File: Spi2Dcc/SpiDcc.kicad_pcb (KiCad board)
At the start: 2 copper layers, 100 x 65 mm, 90 parts, among them P701 LED, P702 Invld cmd out, P703 Mstr SW, P704 Mstr SW bypass, P705 Bstr En Out, P706 Mstr SW out, P801 SPI, P901 Bstr 1, P902 Bstr 2, P903 Bstr 3, P904 Bstr 4, Q701 BC327-40, Q702 BC327-40, Q703 BC327-40, Q901 BC327-40, U201 LM555N, U202 74HC74, U301 74HC4053, U302 74HC32, U401 74HC163, U402 74HC04, U403 74HC163, U404 74HC193, U501 74HC590, U502 74HC75, U503 74HC153, U601 74HC595, U602 74HC165, U603 74HC595, U604 74HC165, U605 74HC595, U606 74HC165, U607 74HC595, U608 74HC165, U609 74HC595, U610 74HC165, U611 74HC595, U612 74HC165

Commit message: Changing the solder mask settings again - based on recommendation found here: http://www.360customs.de/en/2017/01/kicad-elecrow-pcb-service/
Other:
- rule pad_to_mask_clearance: 0.2 -> 0.05
- rule solder_mask_min_width: 0.2 -> 0.1
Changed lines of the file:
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@@
     (pad_size 5 5)
     (pad_drill 3.2)
-    (pad_to_mask_clearance 0.2)
-    (solder_mask_min_width 0.2)
+    (pad_to_mask_clearance 0.05)
+    (solder_mask_min_width 0.1)
     (aux_axis_origin 0 0)
     (visible_elements 7FFFFFFF)
@@
       (drillshape 0)
       (scaleselection 1)
-      (outputdirectory C:/Users/Lars.BEVELDYR/Desktop/SporskiftetBlogBilleder/))
+      (outputdirectory Gerber/))
   )
   (net 0 "")

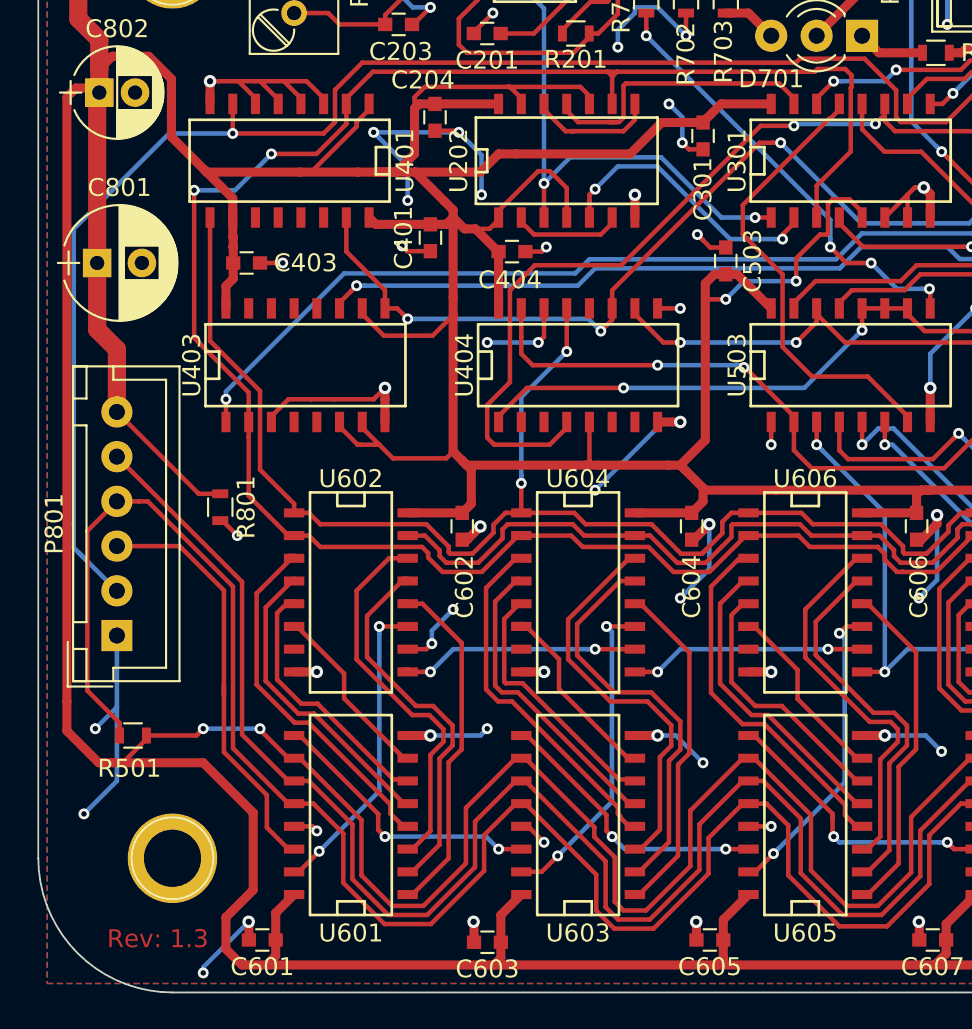
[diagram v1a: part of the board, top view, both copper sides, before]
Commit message: fix command length bits swapped. Connect mounting hole pads to GND.
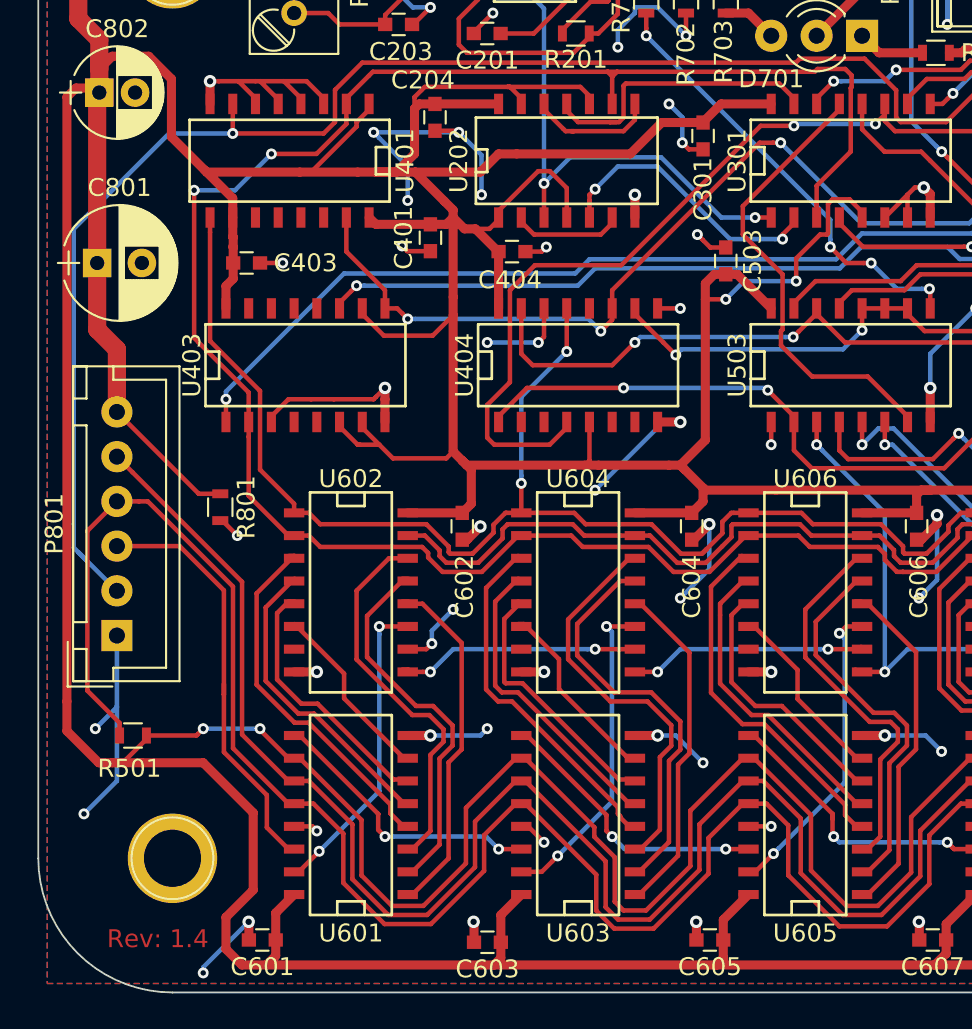
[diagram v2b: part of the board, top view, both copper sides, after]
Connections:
- REF** pad 1: (no net) -> GND (x4)
- U404 pad 1: /DCC State Machine/CMD_LENGTH_BIT_1 -> /Command Register/CMD_LENGTH_BIT_1
- U404 pad 10: /Command Register/CMD_LENGTH_BIT_0 -> /Command Register/CMD_LENGTH_BIT_2
- U404 pad 15: /DCC State Machine/CMD_LENGTH_BIT_0 -> /Command Register/CMD_LENGTH_BIT_0
- U502 pad 10: /DCC State Machine/CMD_LENGTH_BIT_1 -> /Command Register/CMD_LENGTH_BIT_2
- U502 pad 15: /DCC State Machine/CMD_LENGTH_BIT_0 -> /Command Register/CMD_LENGTH_BIT_1
- U503 pad 10: /DCC State Machine/CMD_LENGTH_BIT_1 -> /Command Register/CMD_LENGTH_BIT_2
- U503 pad 11: /DCC State Machine/CMD_LENGTH_BIT_1 -> /Command Register/CMD_LENGTH_BIT_2
- U503 pad 12: /DCC State Machine/CMD_LENGTH_BIT_1 -> /Command Register/CMD_LENGTH_BIT_2
- U503 pad 2: /DCC State Machine/CMD_LENGTH_BIT_0 -> /Command Register/CMD_LENGTH_BIT_1
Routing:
- net /DCC State Machine/CMD_LENGTH_BIT_1: track 47.8 -> 0.00 mm, vias 2 -> 0
- net /DCC State Machine/CMD_LENGTH_BIT_0: track 42.2 -> 0.00 mm, vias 2 -> 0
- net /Command Register/CMD_LENGTH_BIT_1: track 0.00 -> 41.2 mm, vias 0 -> 2
- net /Command Register/CMD_LENGTH_BIT_2: track 0.00 -> 39.7 mm, vias 0 -> 2
- net /Command Register/CMD_LENGTH_BIT_0: track 28.1 -> 36.2 mm
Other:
- board text added: "Rev: 1.4"
- board text removed: "Rev: 1.3"
